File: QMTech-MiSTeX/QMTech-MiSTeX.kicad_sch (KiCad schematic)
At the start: 30 parts, among them J1 RPi_GPIO, J12 Conn_01x03_Pin, J13 USB_C_Receptacle_USB2.0, J2 MiSTer SDRAM Module, J3 USB_C_Receptacle_USB2.0, J4 Conn_02x32_Odd_Even, J5 Conn_02x32_Odd_Even, J6 Conn_01x06_Pin, J7 Conn_01x03_Pin, J8 Conn_01x03_Pin

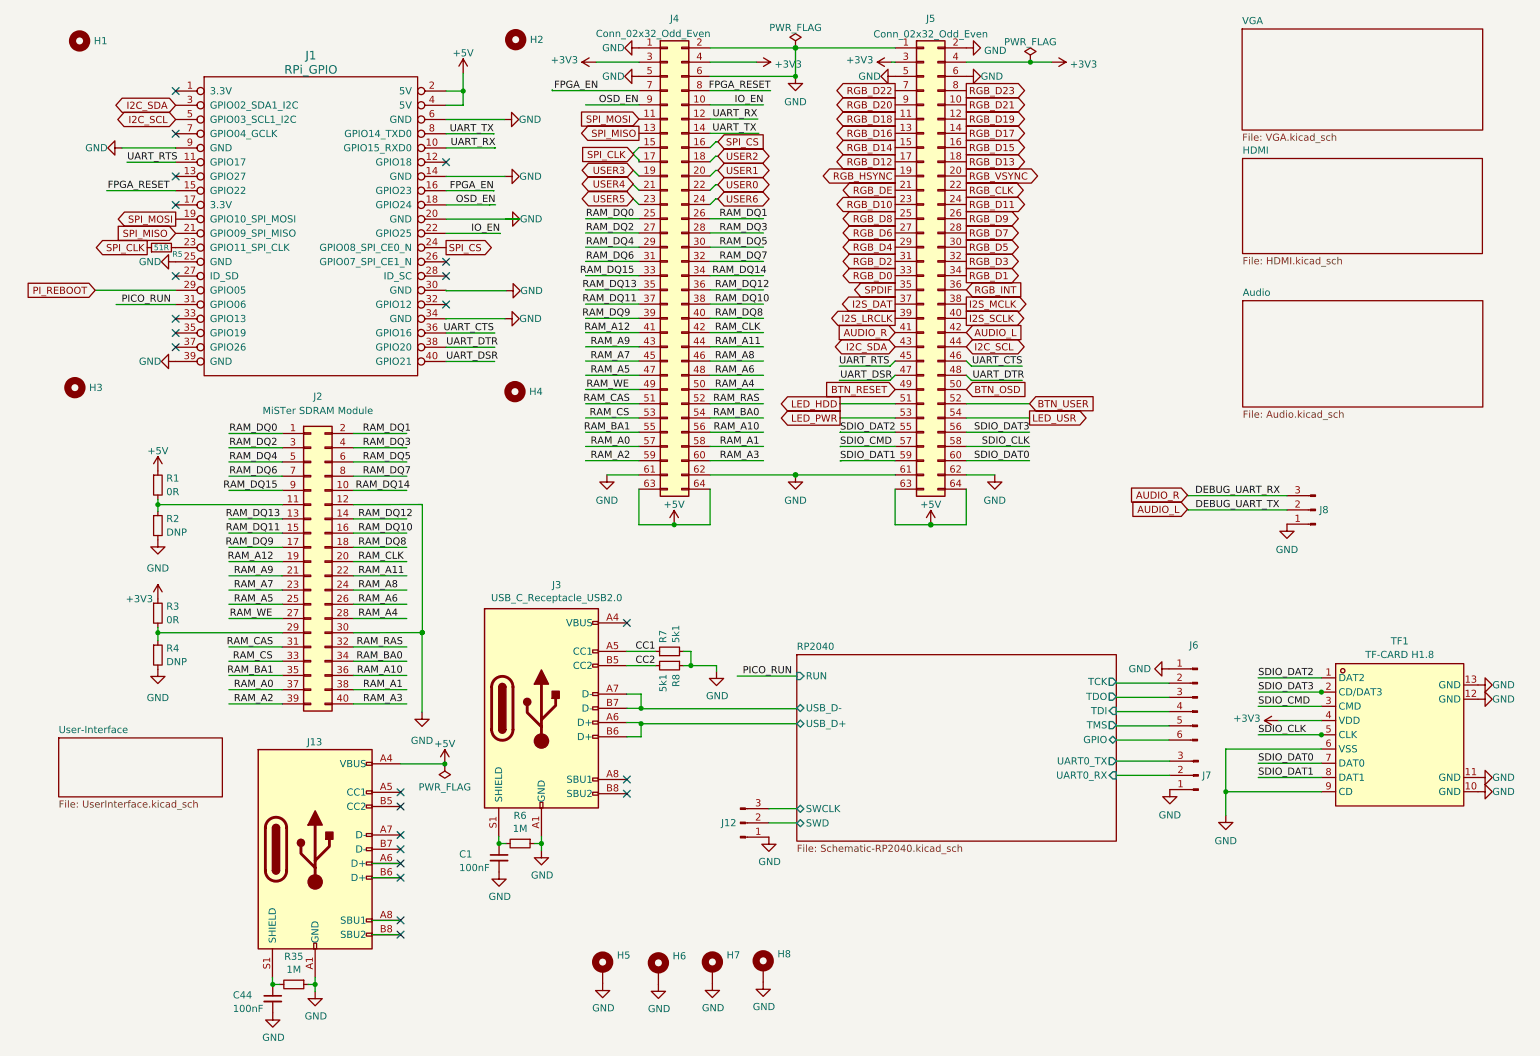
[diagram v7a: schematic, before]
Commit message: add a power switch and break out and break out 4 more GPIOs on RP2040
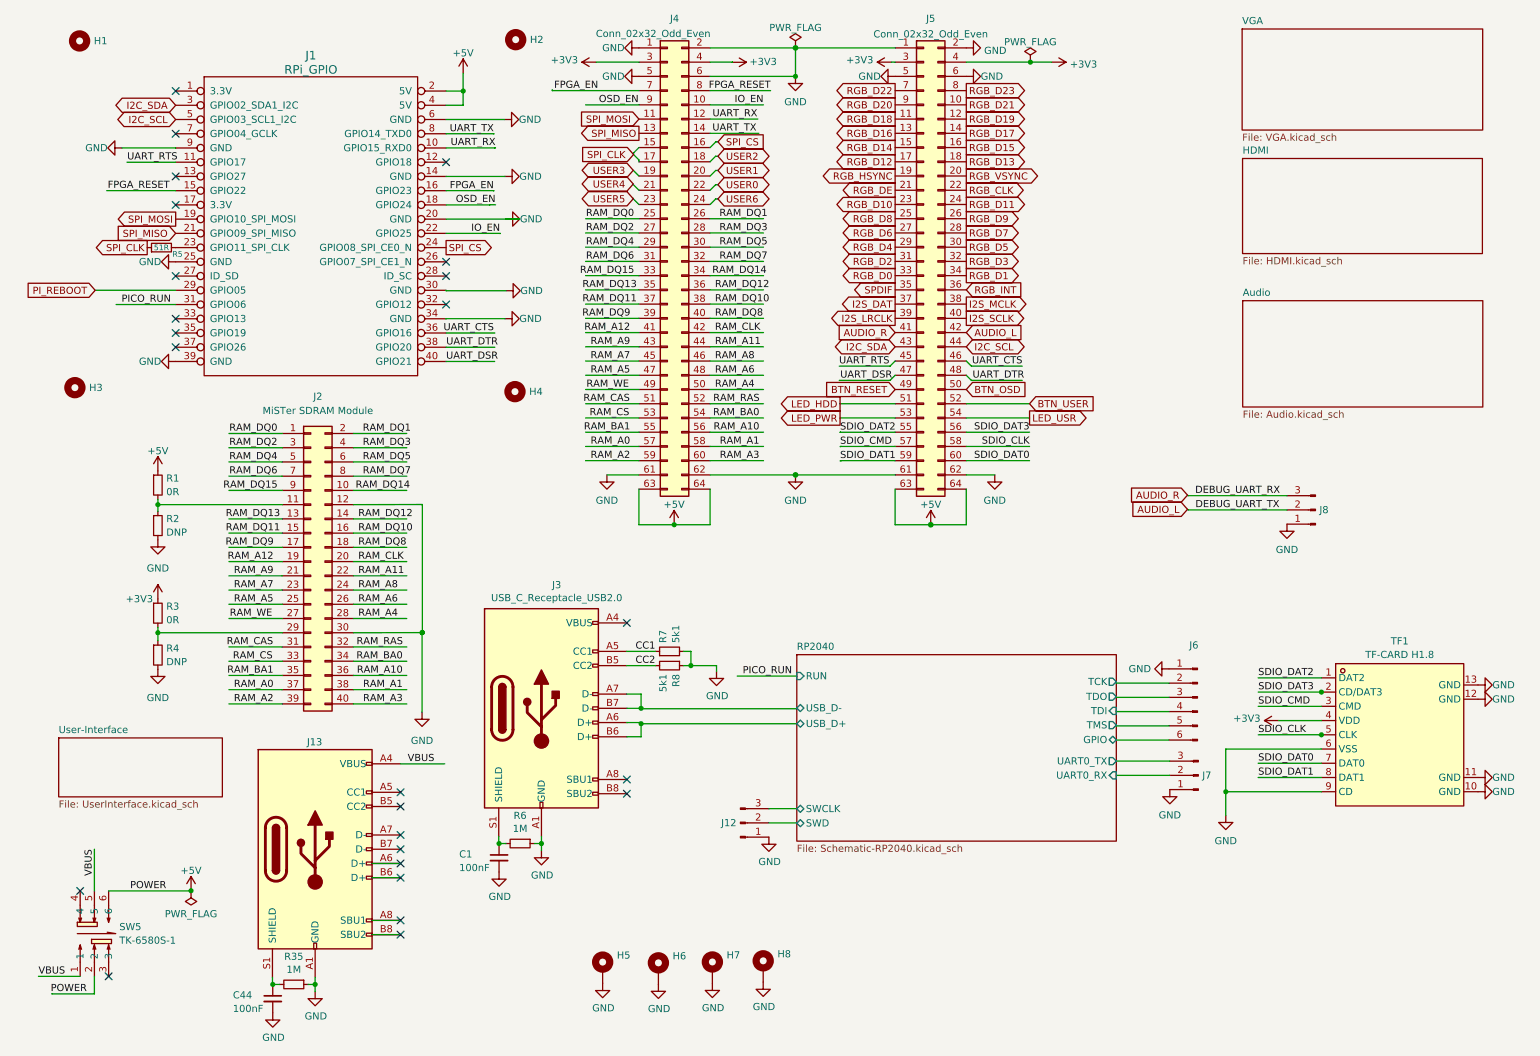
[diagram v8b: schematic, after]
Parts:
- added SW5: TK-6580S-1, easyeda2kicad:SW-SMD_TK-6580S-1, symbol easyeda2kicad:TK-6580S-1
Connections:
- net +5V: now also SW5.2, SW5.6; no longer J13.A4 (VBUS), J13.A9 (VBUS), J13.B4 (VBUS), J13.B9 (VBUS)
- new net VBUS: J13.A4 (VBUS), J13.A9 (VBUS), J13.B4 (VBUS), J13.B9 (VBUS), SW5.1, SW5.5
- no-connect marks 23 -> 25
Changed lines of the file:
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@@
     (company "Hans Baier")
   )
-  (junction (at 88.9254 146.812) (diameter 0) (color 0 0 0 0)
-  )
   (junction (at 84.9122 123.3678) (diameter 0) (color 0 0 0 0)
   )
@@
   (junction (at 193.421 21.5646) (diameter 0) (color 0 0 0 0)
   )
+  (junction (at 43.6372 169.4434) (diameter 0) (color 0 0 0 0)
+  )
   (junction (at 228.2952 151.765) (diameter 0) (color 0 0 0 0)
   )
@@
   (no_connect (at 81.026 154.4066))
   (no_connect (at 81.026 151.8666))
+  (no_connect (at 28.9306 184.7088))
   (no_connect (at 81.026 164.5666))
   (no_connect (at 40.894 26.7208))
@@
   (no_connect (at 81.026 167.1066))
   (no_connect (at 121.412 121.6406))
+  (no_connect (at 23.8506 169.4688))
   (no_connect (at 40.894 72.4408))
   (no_connect (at 40.894 69.9008))
@@
     (stroke (width 0) (type default))
   )
+  (wire (pts (xy 26.3906 184.7088) (xy 26.3906 187.833))
+    (stroke (width 0) (type default))
+  )
   (wire (pts (xy 123.571 97.7646) (xy 123.571 104.1146))
     (stroke (width 0) (type solid))
@@
     (stroke (width 0) (type default))
   )
+  (wire (pts (xy 26.3906 162.0266) (xy 26.3906 169.4688))
+    (stroke (width 0) (type default))
+  )
   (wire (pts (xy 151.511 95.2246) (xy 169.291 95.2246))
     (stroke (width 0) (type solid))
@@
     (stroke (width 0) (type default))
   )
+  (wire (pts (xy 140.2588 21.5646) (xy 136.271 21.5646))
+    (stroke (width 0) (type default))
+  )
   (wire (pts (xy 151.511 19.0246) (xy 169.291 19.0246))
     (stroke (width 0) (type solid))
@@
     (stroke (width 0) (type solid))
   )
+  (wire (pts (xy 140.2588 21.59) (xy 140.2588 21.5646))
+    (stroke (width 0) (type default))
+  )
   (wire (pts (xy 59.9186 105.6132) (xy 50.3936 105.6132))
     (stroke (width 0) (type default))
@@
     (stroke (width 0) (type default))
   )
+  (wire (pts (xy 18.8193 187.833) (xy 18.8193 187.8454))
+    (stroke (width 0) (type default))
+  )
   (wire (pts (xy 228.2952 144.145) (xy 228.2952 151.765))
     (stroke (width 0) (type default))
@@
     (stroke (width 0) (type default))
   )
-  (wire (pts (xy 88.9 146.7866) (xy 88.9254 146.812))
-    (stroke (width 0) (type default))
-  )
   (wire (pts (xy 131.572 129.2606) (xy 132.842 129.2606))
     (stroke (width 0) (type default))
@@
     (stroke (width 0) (type default))
   )
+  (wire (pts (xy 43.6372 169.4688) (xy 43.6372 169.4434))
+    (stroke (width 0) (type default))
+  )
   (wire (pts (xy 121.412 126.7206) (xy 126.492 126.7206))
     (stroke (width 0) (type default))
@@
     (stroke (width 0) (type default))
   )
+  (wire (pts (xy 28.9306 169.4688) (xy 43.6372 169.4688))
+    (stroke (width 0) (type default))
+  )
   (wire (pts (xy 147.066 26.6446) (xy 136.271 26.6446))
     (stroke (width 0) (type default))
@@
     (stroke (width 0) (type default))
   )
+  (wire (pts (xy 18.8193 187.833) (xy 26.3906 187.833))
+    (stroke (width 0) (type default))
+  )
   (wire (pts (xy 208.7626 142.5448) (xy 208.7626 142.494))
     (stroke (width 0) (type default))
@@
     (stroke (width 0) (type default))
   )
-  (wire (pts (xy 136.271 21.5646) (xy 144.526 21.5646))
+  (wire (pts (xy 140.2588 21.59) (xy 140.208 21.59))
     (stroke (width 0) (type default))
   )
@@
     (stroke (width 0) (type default))
   )
+  (wire (pts (xy 16.4084 184.7088) (xy 23.8506 184.7088))
+    (stroke (width 0) (type default))
+  )
   (wire (pts (xy 169.291 21.5646) (xy 168.656 21.5646))
     (stroke (width 0) (type default))
@@
     (effects (font (size 1.27 1.27)) (justify left bottom))
   )
+  (label "POWER" (at 32.7694 169.4688 0) (fields_autoplaced)
+    (effects (font (size 1.27 1.27)) (justify left bottom))
+  )
   (label "UART_CTS" (at 97.6842 69.9008 180) (fields_autoplaced)
     (effects (font (size 1.27 1.27)) (justify right bottom))
@@
     (effects (font (size 1.27 1.27)) (justify left bottom))
   )
+  (label "POWER" (at 25.0444 187.833 180) (fields_autoplaced)
+    (effects (font (size 1.27 1.27)) (justify right bottom))
+  )
   (label "UART_DSR" (at 89.154 74.9808 0) (fields_autoplaced)
     (effects (font (size 1.27 1.27)) (justify left bottom))
@@
     (effects (font (size 1.27 1.27)) (justify left bottom))
   )
+  (label "VBUS" (at 26.3906 162.0266 270) (fields_autoplaced)
+    (effects (font (size 1.27 1.27)) (justify right bottom))
+  )
   (label "RAM_A4" (at 73.4799 120.8532 0) (fields_autoplaced)
     (effects (font (size 1.27 1.27)) (justify left bottom))
@@
     (effects (font (size 1.27 1.27)) (justify right bottom))
   )
+  (label "VBUS" (at 16.4084 184.7088 0) (fields_autoplaced)
+    (effects (font (size 1.27 1.27)) (justify left bottom))
+  )
   (label "RAM_A8" (at 137.1323 74.9046 0) (fields_autoplaced)
     (effects (font (size 1.27 1.27)) (justify left bottom))
@@
     (effects (font (size 1.27 1.27)) (justify right bottom))
   )
+  (label "VBUS" (at 82.2948 146.7866 0) (fields_autoplaced)
+    (effects (font (size 1.27 1.27)) (justify left bottom))
+  )
   (label "DEBUG_UART_RX" (at 237.983 98.933 180) (fields_autoplaced)
     (effects (font (size 1.27 1.27)) (justify right bottom))
@@
     )
   )
+  (symbol (lib_id "easyeda2kicad:TK-6580S-1") (at 26.3906 177.0888 0) (unit 1)
+    (in_bom yes) (on_board yes) (dnp no) (fields_autoplaced)
+    (property "Reference" "SW5" (at 30.8356 175.8767 0)
+      (effects (font (size 1.27 1.27)) (justify left))
+    )
+    (property "Value" "TK-6580S-1" (at 30.8356 178.3009 0)
+      (effects (font (size 1.27 1.27)) (justify left))
+    )
+    (property "Footprint" "easyeda2kicad:SW-SMD_TK-6580S-1" (at 26.3906 192.3288 0)
+      (effects (font (size 1.27 1.27)) hide)
+    )
+    (property "Datasheet" "" (at 26.3906 177.0888 0)
+      (effects (font (size 1.27 1.27)) hide)
+    )
+    (property "LCSC Part" "C528774" (at 26.3906 194.8688 0)
+      (effects (font (size 1.27 1.27)) hide)
+    )
+    (pin "2")
+    (pin "4")
+    (pin "6")
+    (pin "5")
+    (pin "1")
+    (pin "3")
+    (instances
+      (project "QMTech-MiSTeX"
+        (path "/bf95850e-2fcb-4784-a603-f17fc357556b"
+          (reference "SW5") (unit 1)
+        )
+      )
+    )
+  )
   (symbol (lib_id "power:GND") (at 117.094 185.9788 0) (unit 1)
     (in_bom yes) (on_board yes) (dnp no)
@@
     )
   )
-  (symbol (lib_id "power:PWR_FLAG") (at 88.9254 146.812 0) (mirror x) (unit 1)
+  (symbol (lib_id "power:PWR_FLAG") (at 43.6372 169.4434 0) (mirror x) (unit 1)
     (in_bom yes) (on_board yes) (dnp no) (fields_autoplaced)
-    (property "Reference" "#FLG03" (at 88.9254 148.717 0)
+    (property "Reference" "#FLG03" (at 43.6372 171.3484 0)
       (effects (font (size 1.27 1.27)) hide)
     )
-    (property "Value" "PWR_FLAG" (at 88.9254 150.9451 0)
+    (property "Value" "PWR_FLAG" (at 43.6372 173.5765 0)
       (effects (font (size 1.27 1.27)))
     )
-    (property "Footprint" "" (at 88.9254 146.812 0)
+    (property "Footprint" "" (at 43.6372 169.4434 0)
       (effects (font (size 1.27 1.27)) hide)
     )
-    (property "Datasheet" "~" (at 88.9254 146.812 0)
+    (property "Datasheet" "~" (at 43.6372 169.4434 0)
       (effects (font (size 1.27 1.27)) hide)
     )
@@
     )
   )
-  (symbol (lib_id "power:+5V") (at 88.9254 146.812 0) (mirror y) (unit 1)
+  (symbol (lib_id "power:+5V") (at 43.6372 169.4434 0) (mirror y) (unit 1)
     (in_bom yes) (on_board yes) (dnp no) (fields_autoplaced)
-    (property "Reference" "#PWR0151" (at 88.9254 150.622 0)
+    (property "Reference" "#PWR0151" (at 43.6372 173.2534 0)
       (effects (font (size 1.27 1.27)) hide)
     )
-    (property "Value" "+5V" (at 88.9254 143.2074 0)
+    (property "Value" "+5V" (at 43.6372 165.8388 0)
       (effects (font (size 1.27 1.27)))
     )
-    (property "Footprint" "" (at 88.9254 146.812 0)
+    (property "Footprint" "" (at 43.6372 169.4434 0)
       (effects (font (size 1.27 1.27)) hide)
     )
-    (property "Datasheet" "" (at 88.9254 146.812 0)
+    (property "Datasheet" "" (at 43.6372 169.4434 0)
       (effects (font (size 1.27 1.27)) hide)
     )
@@
     )
   )
-  (symbol (lib_id "power:+3V3") (at 144.526 21.5646 270) (unit 1)
+  (symbol (lib_id "power:+3V3") (at 140.208 21.59 270) (unit 1)
     (in_bom yes) (on_board yes) (dnp no)
-    (property "Reference" "#PWR023" (at 140.716 21.5646 0)
+    (property "Reference" "#PWR023" (at 136.398 21.59 0)
       (effects (font (size 1.27 1.27)) hide)
     )
-    (property "Value" "+3V3" (at 147.7772 21.9456 90)
+    (property "Value" "+3V3" (at 143.3068 21.4884 90)
       (effects (font (size 1.27 1.27)) (justify left))
     )
-    (property "Footprint" "" (at 144.526 21.5646 0)
+    (property "Footprint" "" (at 140.208 21.59 0)
       (effects (font (size 1.27 1.27)) hide)
     )
-    (property "Datasheet" "" (at 144.526 21.5646 0)
+    (property "Datasheet" "" (at 140.208 21.59 0)
       (effects (font (size 1.27 1.27)) hide)
     )
